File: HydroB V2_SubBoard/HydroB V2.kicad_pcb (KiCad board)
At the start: 4 copper layers, 89.6 x 101.8 mm, 77 parts, among them J1 FAN, J14 Screw_Terminal_01x02, J15 Screw_Terminal_01x02, J16 Screw_Terminal_01x02, J17 Screw_Terminal_01x02, J18 Screw_Terminal_01x02, J3 Conn_01x02_Pin, J4 Conn_01x04_Pin, J5 PH SENSOR, J6 EC SENSOR, J7 Conn_01x02_Pin, K10 SRD-05VDC-SL-C, K5 SRD-05VDC-SL-C, K7 SRD-05VDC-SL-C, K8 SRD-05VDC-SL-C, K9 SRD-05VDC-SL-C, Q10 S8050, Q6 S8050, Q7 S8050, Q8 S8050, Q9 S8050, SW1 SW_Push, U1 STM32F103C8Tx, U2 TPS5410D, U3 SN65HVD72DR, U4 TPS7A2633DRVR, U5 SN65HVD230, Y1 8Mhz

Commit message: finish the subboard layout
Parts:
- removed D3: B340, Diode_SMD:D_SMA
- removed J3: Conn_01x02_Pin, Connector_Phoenix_MC:PhoenixContact_MCV_1,5_2-G-3.5_1x02_P3.50mm_Vertical
- added C17: 0.1uF, Capacitor_SMD:C_0603_1608Metric, F.Cu at (138.4, 109.8)
- added C18: c, Capacitor_SMD:C_0805_2012Metric, F.Cu at (138.4, 99.6)
- added C19: 22uF, Capacitor_SMD:C_0805_2012Metric, F.Cu at (129.3, 95.5)
- added C20: 22uF, Capacitor_SMD:C_0805_2012Metric, F.Cu at (125.7, 102.5)
- added C21: 22uF, Capacitor_SMD:C_0805_2012Metric, F.Cu at (125.7, 99.5)
- added C22: 22uF, Capacitor_SMD:C_0805_2012Metric, F.Cu at (131.9, 95.5)
- added J2: Conn_01x02_Pin, Connector_JST:JST_XH_B2B-XH-A_1x02_P2.50mm_Vertical, F.Cu at (108.3, 99.3)
- added R18: 9.09k, Resistor_SMD:R_0603_1608Metric, F.Cu at (138.2, 101.8)
- C1: value 4.7uF -> 10uF; footprint Capacitor_SMD:CP_Elec_6.3x5.4_Nichicon -> Capacitor_SMD:C_0805_2012Metric
- C2: value 0.01uF -> 220nF; footprint Capacitor_SMD:C_0603_1608Metric -> Capacitor_SMD:C_0805_2012Metric
- C3: value 47uF -> 1uF; footprint Capacitor_SMD:CP_Elec_6.3x5.4_Nichicon -> Capacitor_SMD:C_0805_2012Metric
- J1: value FAN -> Conn_01x02_Pin; footprint Connector_Phoenix_MC:PhoenixContact_MCV_1,5_2-G-3.5_1x02_P3.50mm_Vertical -> Connector_JST:JST_XH_B2B-XH-A_1x02_P2.50mm_Vertical
- J14, J15, J16, J17, J18: footprint TerminalBlock_Phoenix:TerminalBlock_Phoenix_MKDS-1,5-2-5.08_1x02_P5.08mm_Horizontal -> Connector_Phoenix_MC:PhoenixContact_MC_1,5_2-G-3.81_1x02_P3.81mm_Horizontal
- J4: footprint Connector_JST:JST_PH_B4B-PH-K_1x04_P2.00mm_Vertical -> Connector_JST:JST_XH_B4B-XH-A_1x04_P2.50mm_Vertical
- J5, J6: footprint Connector_Phoenix_MC:PhoenixContact_MCV_1,5_4-G-3.81_1x04_P3.81mm_Vertical -> Connector_Phoenix_MC:PhoenixContact_MC_1,5_4-G-3.81_1x04_P3.81mm_Horizontal
- J7: footprint Connector_Phoenix_MC:PhoenixContact_MCV_1,5_2-G-3.5_1x02_P3.50mm_Vertical -> Connector_Phoenix_MC:PhoenixContact_MCV_1,5_2-G-3.81_1x02_P3.81mm_Vertical
- L1: value 68uH -> 27uH; footprint Inductor_SMD:L_7.3x7.3_H4.5 -> Inductor_SMD:L_7.3x7.3_H3.5
- R2: value 10k -> 100k
- R3: value 1.13k -> 100k
- U2: value TPS5410D -> LMR33620ADDA; footprint TPS5410D:SOIC127P599X175-8N -> Package_SO:Texas_HSOP-8-1EP_3.9x4.9mm_P1.27mm_ThermalVias
- moved J1 38.7 mm to (108.1, 61.5), turned to -90 degrees
- moved J4 22.1 mm to (108.2, 81.8)
- moved C2 19.1 mm to (125.8, 109.8)
- moved R2 17.1 mm to (134.7, 115.3), turned to 0 degrees
- moved H6 10.4 mm to (179.0, 142.0)
- moved H5 10.2 mm to (179.0, 49.5)
- moved U2 8.39 mm to (132.4, 111.1), turned to 0 degrees
- moved D4 8.11 mm to (116.6, 90.7), turned to 90 degrees
- moved J17 7.66 mm to (178.2, 116.8)
- moved J16 7.66 mm to (178.2, 97.3)
- moved J15 7.65 mm to (178.2, 78.0)
- moved J14 7.65 mm to (178.2, 59.0)
- moved J18 7.59 mm to (178.3, 136.7)
- moved R20 6.88 mm to (118.8, 90.8), turned to 90 degrees
- moved C9 5.47 mm to (121.0, 91.9), turned to 90 degrees
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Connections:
- C2 pad 1: Net-(D3-K) -> +24V
- C2 pad 2: Net-(U2-BOOT) -> GND
- C3 pad 1: +12V -> Net-(U2-VCC)
- J1 pad 1: GND -> Net-(J1-Pin_1)
- J1 pad 2: +12V -> Net-(J1-Pin_2)
- J4 pad 1: SWDIO -> GND
- J4 pad 2: SWCLK -> +3.3V
- J4 pad 3: +3.3V -> SWDIO
- J4 pad 4: GND -> SWCLK
- L1 pad 1: +12V -> Net-(U2-SW)
- L1 pad 2: Net-(D3-K) -> +12V
- R17 pad 1: Net-(J3-Pin_1) -> Net-(J1-Pin_1)
- R17 pad 2: Net-(J3-Pin_2) -> Net-(J1-Pin_2)
- R2 pad 1: Net-(U2-VSENSE) -> PG
- R2 pad 2: +12V -> Net-(U2-VCC)
- R3 pad 1: GND -> Net-(U2-FB)
- R3 pad 2: Net-(U2-VSENSE) -> +12V
- U2 pad 1: Net-(U2-BOOT) -> GND
- U2 pad 2: (no net) -> +24V
- U2 pad 3: (no net) -> +24V
- U2 pad 4: Net-(U2-VSENSE) -> PG
- U2 pad 5: ENA -> Net-(U2-FB)
- U2 pad 6: GND -> Net-(U2-VCC)
- U2 pad 7: +24V -> Net-(U2-BOOT)
- U2 pad 8: Net-(D3-K) -> Net-(U2-SW)
- U5 pad 6: Net-(J3-Pin_1) -> Net-(J1-Pin_1)
- U5 pad 7: Net-(J3-Pin_2) -> Net-(J1-Pin_2)
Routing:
- net Net-(J3-Pin_1): track 34.1 -> 0.00 mm
- net Net-(J3-Pin_2): track 29.1 -> 0.00 mm
- net Net-(J1-Pin_1): track 0.00 -> 24.5 mm
- net Net-(U2-FB): track 0.00 -> 19.8 mm, vias 0 -> 2
- net Net-(D3-K): track 18.4 -> 0.00 mm
- net SWCLK: track 41.1 -> 23.5 mm, vias 1 -> 0
- net SWDIO: track 36.8 -> 20.3 mm, vias 1 -> 0
- net Net-(J1-Pin_2): track 0.00 -> 13.4 mm
- net N: track 23.3 -> 34.6 mm
- net +24V: track 139.8 -> 149.6 mm
- net +12V: track 38.3 -> 48.0 mm, vias 8 -> 6
- net Net-(U2-SW): track 0.00 -> 9.25 mm
- net Net-(U2-VCC): track 0.00 -> 8.65 mm
- net Net-(J17-Pin_2): track 29.8 -> 21.8 mm
- net Net-(J15-Pin_2): track 29.8 -> 22.1 mm
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- added copper zone on F.Cu, net +12V
- removed copper zone on F.Cu, net GND
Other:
- board size 89.6 x 101.8 mm -> 79 x 100.5 mm

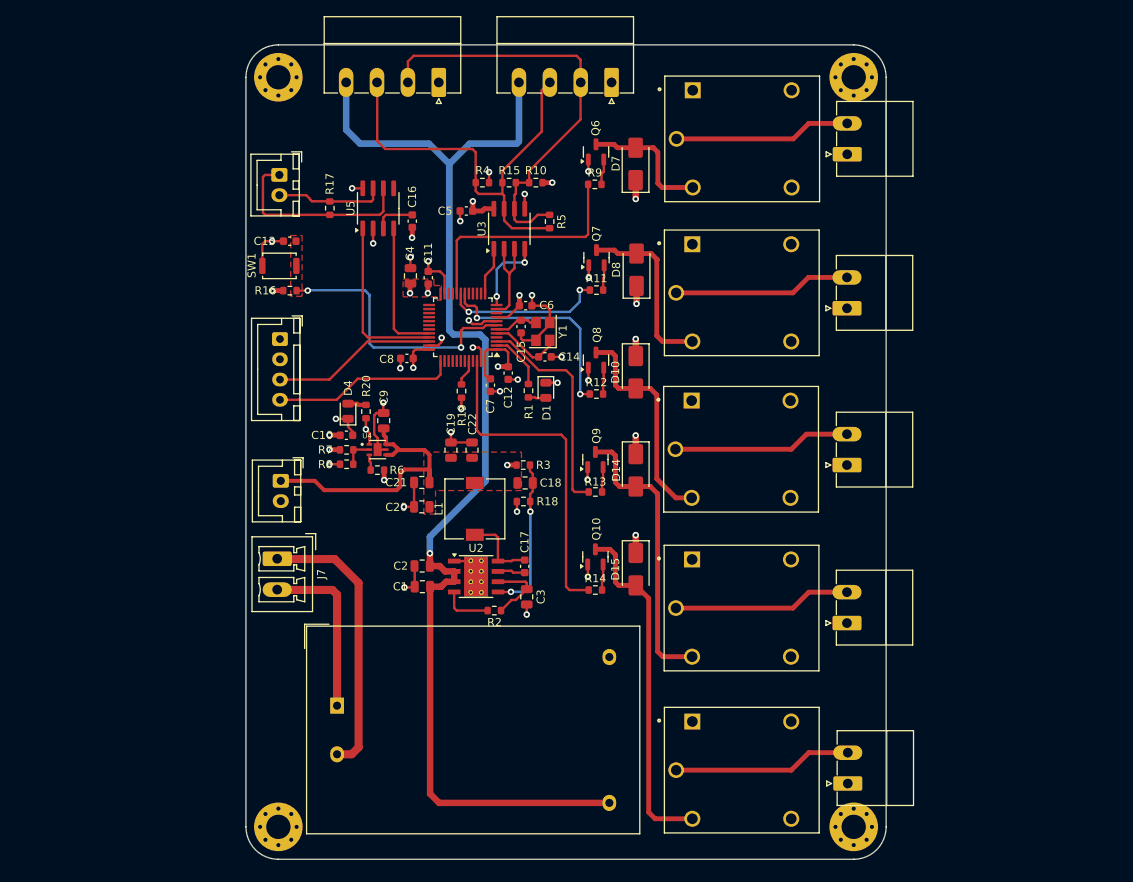
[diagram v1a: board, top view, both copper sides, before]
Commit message: subboard updated for PCB placement
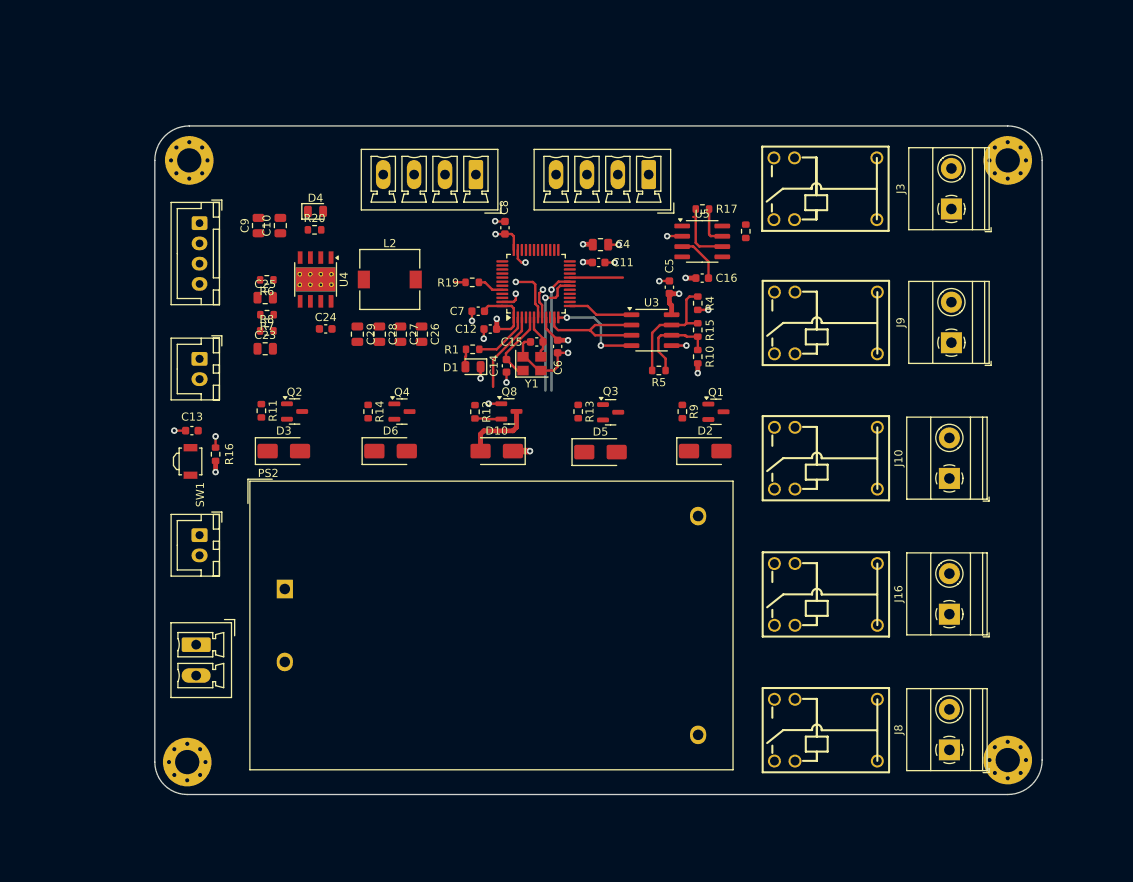
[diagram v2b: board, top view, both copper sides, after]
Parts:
- removed C1: 10uF, Capacitor_SMD:C_0805_2012Metric
- removed C17: 0.1uF, Capacitor_SMD:C_0603_1608Metric
- removed C18: c, Capacitor_SMD:C_0805_2012Metric
- removed C19, C20, C21, C22: 22uF, Capacitor_SMD:C_0805_2012Metric
- removed C2: 220nF, Capacitor_SMD:C_0805_2012Metric
- removed C3: 1uF, Capacitor_SMD:C_0805_2012Metric
- removed D14, D15, D7, D8: 1N4007, Diode_SMD:D_SMA
- removed J14, J15, J17, J18: Screw_Terminal_01x02, Connector_Phoenix_MC:PhoenixContact_MC_1,5_2-G-3.81_1x02_P3.81mm_Horizontal
- removed K10, K5, K7, K8, K9: SRD-05VDC-SL-C, SRD-05VDC-SL-C (1):RELAY_SRD-05VDC-SL-C
- removed L1: 27uH, Inductor_SMD:L_7.3x7.3_H3.5
- removed Q10, Q6, Q7, Q9: S8050, Package_TO_SOT_SMD:SOT-23
- removed R18: 9.09k, Resistor_SMD:R_0603_1608Metric
- removed R2, R3: 100k, Resistor_SMD:R_0603_1608Metric
- removed U2: LMR33620ADDA, Package_SO:Texas_HSOP-8-1EP_3.9x4.9mm_P1.27mm_ThermalVias
- added C23: 1uF, Capacitor_SMD:C_0805_2012Metric, F.Cu at (106.4, 83.0)
- added C24: 100NF, Capacitor_SMD:C_0603_1608Metric, F.Cu at (113.8, 80.5)
- added C25: c, Capacitor_SMD:C_0805_2012Metric, F.Cu at (106.4, 76.7)
- added C26: 22uF, Capacitor_SMD:C_0805_2012Metric, F.Cu at (125.7, 81.2)
- added C27: 22uF, Capacitor_SMD:C_0805_2012Metric, F.Cu at (123.1, 81.2)
- added C28: 22uF, Capacitor_SMD:C_0805_2012Metric, F.Cu at (120.5, 81.2)
- added C29: 22uF, Capacitor_SMD:C_0805_2012Metric, F.Cu at (117.8, 81.2)
- added D2: 1N4007, Diode_SMD:D_SMA, F.Cu at (160.7, 95.6)
- added D3: 1N4007, Diode_SMD:D_SMA, F.Cu at (108.7, 95.6)
- added D5: 1N4007, Diode_SMD:D_SMA, F.Cu at (147.8, 95.8)
- added D6: 1N4007, Diode_SMD:D_SMA, F.Cu at (121.8, 95.6)
- added J10: Screw_Terminal_01x02, TerminalBlock_Phoenix:TerminalBlock_Phoenix_MKDS-1,5-2_1x02_P5.00mm_Horizontal, F.Cu at (190.8, 99.0)
- added J3: Screw_Terminal_01x02, TerminalBlock_Phoenix:TerminalBlock_Phoenix_MKDS-1,5-2_1x02_P5.00mm_Horizontal, F.Cu at (191.1, 65.8)
- added J8: Screw_Terminal_01x02, TerminalBlock_Phoenix:TerminalBlock_Phoenix_MKDS-1,5-2_1x02_P5.00mm_Horizontal, F.Cu at (190.8, 132.5)
- added J9: Screw_Terminal_01x02, TerminalBlock_Phoenix:TerminalBlock_Phoenix_MKDS-1,5-2_1x02_P5.00mm_Horizontal, F.Cu at (191.1, 82.2)
- added L2: 10uH, Inductor_SMD:L_7.3x7.3_H3.5, F.Cu at (121.8, 74.5)
- added Q1: S8050, Package_TO_SOT_SMD:SOT-23, F.Cu at (162.0, 90.8)
- added Q2: S8050, Package_TO_SOT_SMD:SOT-23, F.Cu at (110.0, 90.7)
- added Q3: S8050, Package_TO_SOT_SMD:SOT-23, F.Cu at (149.0, 90.8)
- added Q4: S8050, Package_TO_SOT_SMD:SOT-23, F.Cu at (123.2, 90.8)
- added R21: 10k, Resistor_SMD:R_0603_1608Metric, F.Cu at (165.7, 68.5)
- added U10: ~, relay 12vdc 3A:RELAY-TH_SRS-12VDC-SL, F.Cu at (175.6, 96.5)
- added U6: ~, relay 12vdc 3A:RELAY-TH_SRS-12VDC-SL, F.Cu at (175.6, 113.3)
- added U7: ~, relay 12vdc 3A:RELAY-TH_SRS-12VDC-SL, F.Cu at (175.5, 63.3)
- added U8: ~, relay 12vdc 3A:RELAY-TH_SRS-12VDC-SL, F.Cu at (175.6, 130.1)
- added U9: ~, relay 12vdc 3A:RELAY-TH_SRS-12VDC-SL, F.Cu at (175.6, 79.8)
- C10: value 1uF -> 220nF; footprint Capacitor_SMD:C_0603_1608Metric -> Capacitor_SMD:C_0805_2012Metric
- C9: value 1uF -> 10uF
- J16: footprint Connector_Phoenix_MC:PhoenixContact_MC_1,5_2-G-3.81_1x02_P3.81mm_Horizontal -> TerminalBlock_Phoenix:TerminalBlock_Phoenix_MKDS-1,5-2_1x02_P5.00mm_Horizontal
- J5, J6: footprint Connector_Phoenix_MC:PhoenixContact_MC_1,5_4-G-3.81_1x04_P3.81mm_Horizontal -> Connector_Phoenix_MC:PhoenixContact_MCV_1,5_4-G-3.81_1x04_P3.81mm_Vertical
- PS2: value HLK-5M24 -> HLK-20M12; footprint Converter_ACDC:Converter_ACDC_Hi-Link_HLK-5Mxx -> Converter_ACDC:Converter_ACDC_Hi-Link_HLK-20Mxx
- R11, R12, R13, R14, R9: value 470 -> 1K
- R6: value 10K -> 100k
- R7: value 1.96M -> 100k
- R8: value 1.18M -> 43.2k
- SW1: footprint Button_Switch_SMD:SW_Push_SPST_NO_Alps_SKRK -> Button_Switch_SMD:SW_SPST_B3U-3000P
- U4: value TPS7A2633DRVR -> LMR33620ADDA; footprint TPS7A2633DRVR:SON65P200X200X80-7N -> Package_SO:Texas_HSOP-8-1EP_3.9x4.9mm_P1.27mm_ThermalVias
- moved R17 46.0 mm to (160.3, 65.8), turned to 0 degrees
- moved R11 44.0 mm to (105.9, 90.7), turned to -90 degrees
- moved U5 40.2 mm to (160.3, 69.8), turned to 0 degrees
- moved C16 36.5 mm to (160.3, 74.3), turned to 0 degrees
- moved R14 35.7 mm to (119.1, 90.8), turned to -90 degrees
- moved R4 30.5 mm to (159.8, 77.4), turned to -90 degrees
- moved R9 30.0 mm to (157.9, 90.8), turned to -90 degrees
- moved R15 29.5 mm to (159.8, 80.7), turned to 90 degrees
- moved R10 29.3 mm to (159.8, 84.0), turned to 90 degrees
- moved C9 28.6 mm to (105.5, 67.8)
- moved R6 27.2 mm to (106.6, 74.5), turned to 180 degrees
- moved C10 27.1 mm to (108.2, 67.8), turned to 90 degrees
- moved C5 26.8 mm to (156.3, 75.4), turned to 90 degrees
- moved SW1 26.5 mm to (97.2, 96.9), turned to 90 degrees
- moved C13 26.3 mm to (97.3, 93.1)
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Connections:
- C10 pad 1: +3.3V -> +12V
- J16 pad 1: GND -> Net-(J16-Pin_1)
- J16 pad 2: Net-(J16-Pin_2) -> GND
- J5 pad 4: +24V -> +12V
- J6 pad 4: +24V -> +12V
- PS2 pad 4: +24V -> +12V
- R11 pad 1: /HydroB/Block Relay1/RELAY_4 -> /HydroB/Block Relay1/RELAY_3
- R13 pad 1: /HydroB/Block Relay1/RELAY_5 -> /HydroB/Block Relay1/RELAY_4
- R14 pad 1: /HydroB/Block Relay1/RELAY_3 -> /HydroB/Block Relay1/RELAY_5
- R6 pad 1: Net-(U4-PG) -> PG
- R6 pad 2: +3.3V -> Net-(U4-VCC)
- R7 pad 1: +3.3V -> Net-(U4-FB)
- R7 pad 2: Net-(U4-NC) -> +3.3V
- R8 pad 1: Net-(U4-NC) -> GND
- R8 pad 2: GND -> Net-(U4-FB)
- U4 pad 1: +3.3V -> GND
- U4 pad 2: Net-(U4-NC) -> +12V
- U4 pad 3: Net-(U4-PG) -> +12V
- U4 pad 4: +12V -> PG
- U4 pad 5: GND -> Net-(U4-FB)
- U4 pad 6: +12V -> Net-(U4-VCC)
- U4 pad 7: GND -> Net-(U4-BOOT)
- U5 pad 8: GND -> Net-(U5-Rs)
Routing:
- net +24V: track 149.6 -> 0.00 mm, vias 1 -> 0
- net +12V: track 48.0 -> 2.10 mm, vias 6 -> 1
- net GND: track 84.3 -> 38.8 mm, vias 31 -> 17
- net Net-(D15-A): track 43.2 -> 0.00 mm
- net Net-(J5-Pin_2): track 53.3 -> 11.1 mm
- net /HydroB/Block Relay1/RELAY_3: track 41.2 -> 0.00 mm
- net Net-(J5-Pin_3): track 53.7 -> 15.2 mm
- net Net-(D14-A): track 35.7 -> 0.00 mm
- net N: track 34.6 -> 0.00 mm
- net NRST: track 33.6 -> 8.19 mm
- net SWCLK: track 23.5 -> 0.00 mm
- net /HydroB/Block Relay1/RELAY_1: track 29.2 -> 6.55 mm
- net Net-(J16-Pin_2): track 22.1 -> 0.00 mm
- net Net-(D8-A): track 22.1 -> 0.00 mm
- net Net-(J18-Pin_2): track 22.1 -> 0.00 mm
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- removed copper zone on F.Cu, net +12V
- removed copper zone on In2.Cu, net +12V
- removed copper zone on F.Cu, net +3.3V
- removed copper zone on In2.Cu, net +3.3V
- removed copper zone on F.Cu, net NRST
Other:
- board size 79 x 100.5 mm -> 109.5 x 82.5 mm

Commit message: PCB layout update
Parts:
- added G***: LOGO, CHIPTREE_LOGO:cam5x5, F.Cu at (123.0, 108.2)
- added G***: LOGO, CHIPTREE_LOGO:CHPTREE-5x5mm, F.Cu at (128.6, 108.7)
- C9: footprint Capacitor_SMD:C_0805_2012Metric -> Capacitor_SMD:CP_Elec_4x3
- SW1: footprint Button_Switch_SMD:SW_SPST_B3U-3000P -> Button_Switch_THT:SW_Tactile_SPST_Angled_PTS645Vx39-2LFS
- moved H5 111.9 mm to (86.2, 63.8)
- moved H6 111.8 mm to (86.2, 133.0)
- moved J9 102.9 mm to (93.8, 115.8)
- moved J10 102.1 mm to (93.8, 131.0)
- moved J8 102.1 mm to (93.8, 100.7)
- moved J16 101.6 mm to (93.8, 85.8)
- moved J3 97.4 mm to (93.8, 70.8)
- moved J4 95.4 mm to (169.4, 131.1), turned to 0 degrees
- moved J1 95.0 mm to (183.7, 125.7), turned to 90 degrees
- moved H8 92.9 mm to (189.6, 133.0)
- moved H7 92.7 mm to (189.6, 63.8)
- moved J7 87.2 mm to (184.1, 107.0), turned to 90 degrees
- moved J2 86.1 mm to (183.7, 116.6), turned to 90 degrees
- moved C9 80.4 mm to (175.0, 108.2), turned to 0 degrees
- moved D4 79.6 mm to (176.0, 114.1)
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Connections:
- U1 pad 18: /HydroB/Block Relay1/RELAY_2 -> unconnected-(U1-PB0-Pad18)
- U1 pad 19: /HydroB/Block Relay1/RELAY_4 -> unconnected-(U1-PB1-Pad19)
- U1 pad 20: /HydroB/Block Relay1/RELAY_1 -> unconnected-(U1-PB2-Pad20)
- U1 pad 40: unconnected-(U1-PB4-Pad40) -> /HydroB/Block Relay1/RELAY_1
- U1 pad 41: unconnected-(U1-PB5-Pad41) -> /HydroB/Block Relay1/RELAY_2
- U1 pad 43: unconnected-(U1-PB7-Pad43) -> /HydroB/Block Relay1/RELAY_3
- U1 pad 45: unconnected-(U1-PB8-Pad45) -> /HydroB/Block Relay1/RELAY_4
- U1 pad 46: /HydroB/Block Relay1/RELAY_3 -> unconnected-(U1-PB9-Pad46)
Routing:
- net +12V: track 2.10 -> 117.0 mm
- net NRST: track 8.19 -> 73.6 mm
- net SWCLK: track 0.00 -> 63.5 mm, vias 0 -> 1
- net SWDIO: track 0.00 -> 48.9 mm, vias 0 -> 1
- net Net-(J5-Pin_2): track 11.1 -> 53.3 mm
- net /HydroB/Block Relay1/RELAY_1: track 6.55 -> 46.2 mm
- net N: track 0.00 -> 37.9 mm
- net Net-(J1-Pin_2): track 4.84 -> 40.8 mm, vias 0 -> 1
- net Net-(J1-Pin_1): track 7.64 -> 41.3 mm, vias 0 -> 1
- net +3.3V: track 28.8 -> 59.9 mm, vias 9 -> 12
- net Net-(J5-Pin_3): track 15.2 -> 45.5 mm, vias 0 -> 1
- net PG: track 0.00 -> 20.0 mm
- net /HydroB/Block Relay1/RELAY_3: track 0.00 -> 19.1 mm
- net Net-(D2-A): track 0.00 -> 18.3 mm
- net L: track 0.00 -> 18.2 mm
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- added copper zone on In2.Cu, net +12V
- added copper zone on F.Cu, net +3.3V
- added copper zone on In2.Cu, net +3.3V
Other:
- board size 109.5 x 82.5 mm -> 110.6 x 76.4 mm
- board text added: "12V"
- board text added: "3.3V"
- board text added: "A"
- board text added: "B"
- board text added: "CLK"
- board text added: "DIO"
- board text added: "GND"
- board text added: "H"
- board text added: "L"
- board text added: "Made in Cambodia"
- board text added: "PC13"
- board text added: "POWER LED"
- board text added: "RESET"

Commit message: PCB update finalize
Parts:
- moved C26 5.57 mm to (174.5, 124.2), turned to -90 degrees
- moved C27 4.35 mm to (172.3, 124.2), turned to -90 degrees
- moved C10 1.30 mm to (175.3, 104.5)
- moved C28 0.78 mm to (170.0, 124.2)
- moved C14 0.15 mm to (136.4, 123.1), turned to 90 degrees
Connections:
- C16 pad 1: +3.3V -> GND
- C16 pad 2: Net-(U5-VCC) -> +3.3V
- U5 pad 3: Net-(U5-VCC) -> +3.3V
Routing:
- net +3.3V: track 59.9 -> 207.4 mm, vias 12 -> 9
- net N: track 37.9 -> 0.00 mm
- net L: track 18.2 -> 0.00 mm
- net +12V: track 117.0 -> 128.3 mm
- net Net-(U4-SW): track 12.7 -> 3.85 mm
- net Net-(U5-VCC): track 3.36 -> 0.00 mm
- net GND: track 56.1 -> 57.2 mm, vias 35 -> 700
- added copper zone on F.Cu, net L
- added copper zone on F.Cu, net N
- added copper zone on F.Cu, net Net-(U4-SW)
- removed copper zone on In2.Cu, net +3.3V

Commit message: Subboard updated
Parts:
- moved C6 1.36 mm to (133.5, 107.2), turned to 135 degrees
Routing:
- net +12V: track 128.3 -> 0.15 mm, vias 1 -> 33
- net +3.3V: track 207.4 -> 137.7 mm, vias 9 -> 31
- net Net-(U4-FB): track 9.22 -> 3.11 mm
- net GND: track 57.2 -> 60.3 mm, vias 700 -> 27
- net Net-(D2-A): track 18.3 -> 15.9 mm
- net Net-(D10-A): track 18.0 -> 16.3 mm
- net PG: track 20.0 -> 18.5 mm
- net NRST: track 73.6 -> 74.4 mm
- added copper zone on F.Cu, net +12V
- added copper zone on In2.Cu, net +3.3V
- added copper zone on B.Cu, net GND
- added copper zone on F.Cu, net GND
- added copper zone on In2.Cu, net GND
- added copper zone on F.Cu, net Net-(U4-FB)

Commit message: PCB updated
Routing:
- net GND: track 60.3 -> 23.3 mm, vias 27 -> 472
- net +3.3V: track 137.7 -> 123.7 mm
- net Net-(J5-Pin_2): track 53.3 -> 55.0 mm

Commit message: Subboard updated
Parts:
- added R18: 10K, Resistor_SMD:R_0603_1608Metric, F.Cu at (123.3, 74.8)
- added R2: 10K, Resistor_SMD:R_0603_1608Metric, F.Cu at (123.2, 103.4)
- added R22: 10K, Resistor_SMD:R_0603_1608Metric, F.Cu at (123.4, 117.1)
- added R23: 10K, Resistor_SMD:R_0603_1608Metric, F.Cu at (123.4, 130.9)
- added R3: 10K, Resistor_SMD:R_0603_1608Metric, F.Cu at (123.2, 89.6)
- moved R20 15.1 mm to (170.9, 126.2), turned to 180 degrees
- moved D4 11.3 mm to (170.7, 124.0), turned to 180 degrees
- moved C27 10.7 mm to (176.3, 114.3), turned to 0 degrees
- moved C29 10.1 mm to (176.3, 118.8), turned to 0 degrees
- moved C28 9.93 mm to (176.3, 116.6), turned to 0 degrees
- moved C10 3.67 mm to (175.0, 108.2)
- moved C9 3.63 mm to (175.5, 104.6)
- moved C26 3.57 mm to (176.3, 121.2), turned to 0 degrees
- moved L2 1.70 mm to (168.8, 118.5), turned to 0 degrees
- moved R13 1.29 mm to (125.3, 117.1), turned to 90 degrees
- moved R14 1.28 mm to (125.3, 130.9), turned to 90 degrees
- moved R9 1.23 mm to (125.2, 74.8), turned to 90 degrees
- moved R12 1.23 mm to (125.1, 89.6), turned to 90 degrees
- moved R11 1.21 mm to (125.1, 103.4), turned to 90 degrees
- moved Q3 0.79 mm to (124.4, 113.0)
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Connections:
- net Net-(U4-SW) renamed A
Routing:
- net +3.3V: track 123.7 -> 107.7 mm, vias 31 -> 42
- net GND: track 23.3 -> 18.3 mm, vias 472 -> 454
- net Net-(Q8-B): track 4.14 -> 0.00 mm
- net Net-(Q4-B): track 4.11 -> 0.00 mm
- net Net-(Q2-B): track 4.06 -> 0.00 mm
- net Net-(Q1-B): track 4.05 -> 0.00 mm
- net Net-(Q3-B): track 3.91 -> 0.00 mm
- net SWDIO: track 49.3 -> 47.7 mm
- net PG: track 18.5 -> 19.5 mm
- net NRST: track 74.4 -> 75.4 mm
- net /HydroB/Block Relay1/RELAY_1: track 46.2 -> 45.5 mm
- net /HydroB/Block Relay1/RELAY_5: track 23.3 -> 22.7 mm
- net /HydroB/Block Relay1/RELAY_3: track 19.1 -> 18.6 mm
- net /HydroB/Block Relay1/RELAY_2: track 32.0 -> 31.5 mm
- net +12V: vias 33 -> 40
- added copper zone on F.Cu, net Net-(Q1-B)
- added copper zone on F.Cu, net Net-(Q2-B)
- added copper zone on F.Cu, net Net-(Q3-B)
- added copper zone on F.Cu, net Net-(Q4-B)
- added copper zone on F.Cu, net Net-(Q8-B)
